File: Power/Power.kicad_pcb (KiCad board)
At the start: 2 copper layers, 34.8 x 23.1 mm, 53 parts, among them J1 Conn_01x04_Pin, J2 Conn_01x02, J3 Conn_01x06, J5 GND, J6 +BATT, Q2 AO3400A, Q3 AO3400A, Q4 AO3400A, U1 TPS54331DR, U2 XAL4030-682MEC, U3 TPS54331DR, U4 XAL4030-682MEC

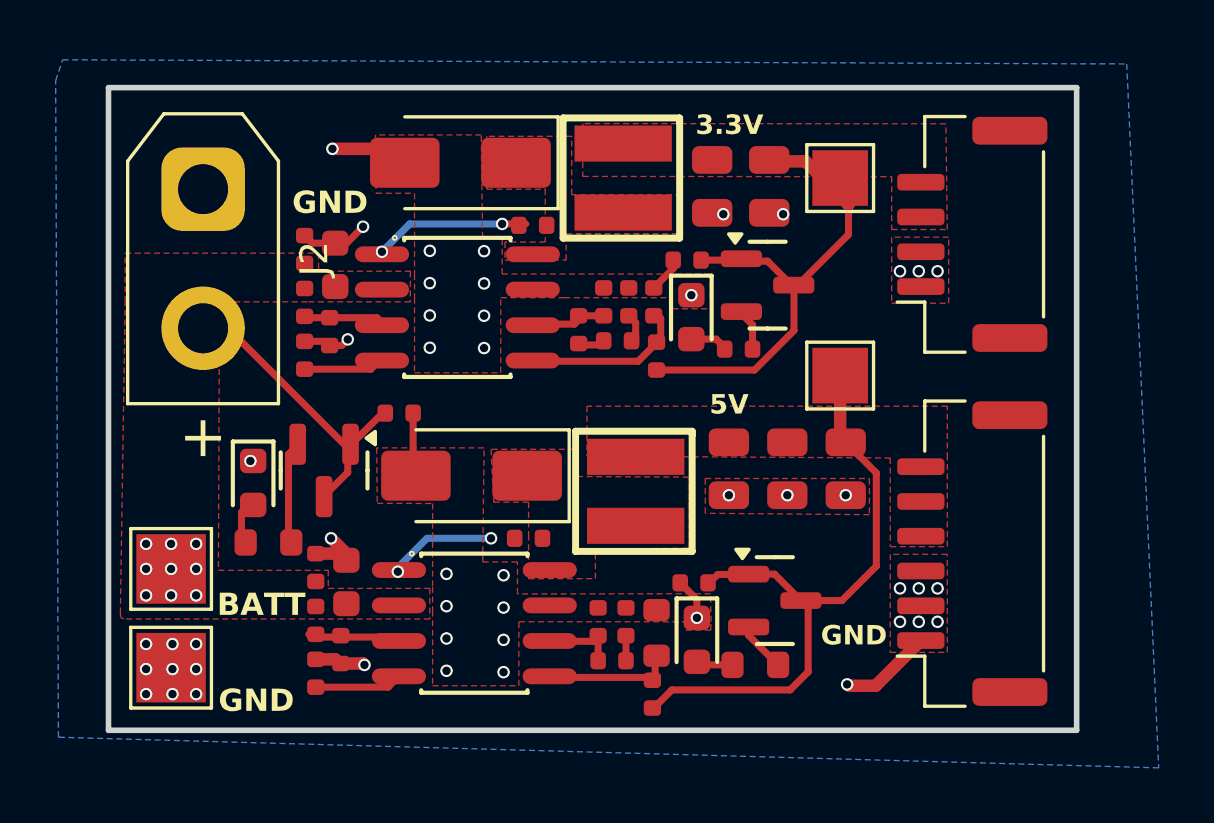
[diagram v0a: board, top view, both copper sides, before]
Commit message: feat: Added mounting holes, text and more connectors for PMU
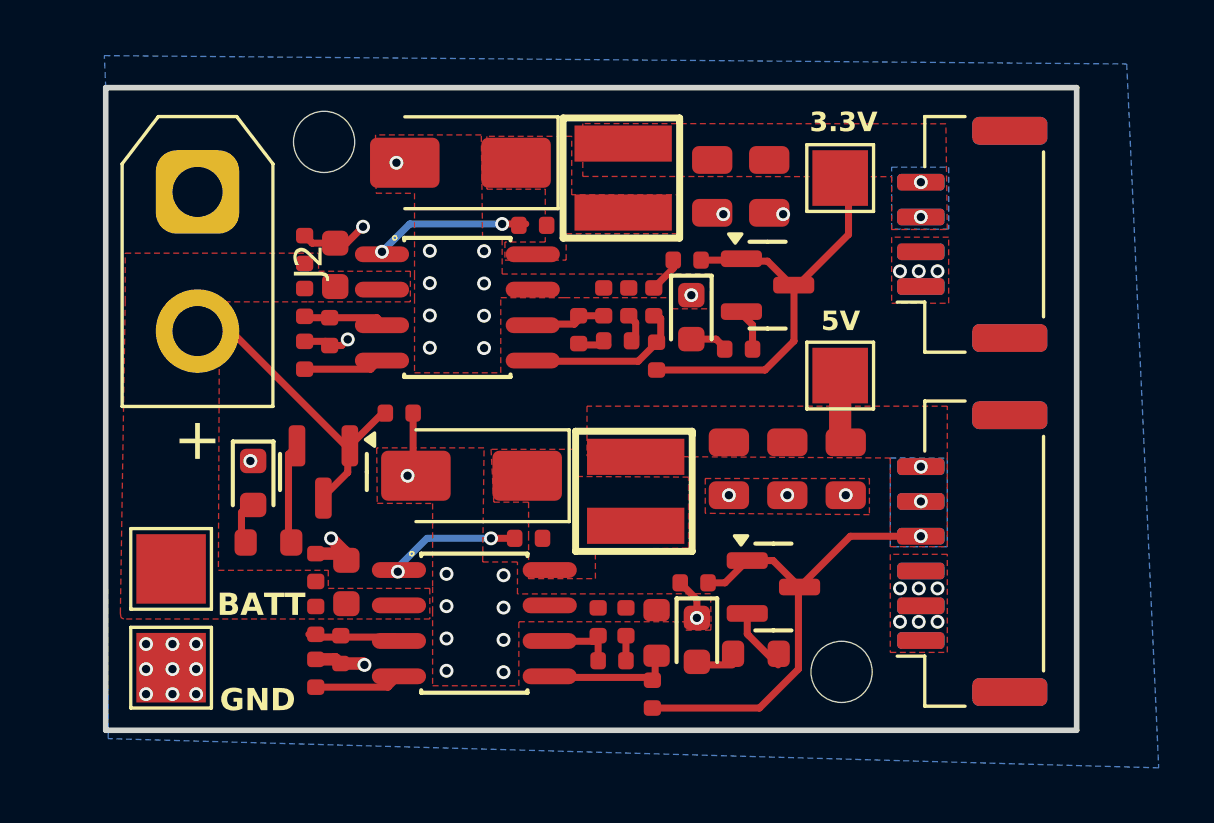
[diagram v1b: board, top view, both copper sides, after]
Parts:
- added ?: , , F.Cu at (121.0, 100.2)
- added ?: , , F.Cu at (102.4, 81.2)
- added J4: Conn_01x04_Pin, Connector_JST:JST_GH_SM04B-GHS-TB_1x04-1MP_P1.25mm_Horizontal, B.Cu at (125.7, 84.5)
- added J7: Conn_01x06, Connector_JST:JST_GH_SM06B-GHS-TB_1x06-1MP_P1.25mm_Horizontal, B.Cu at (125.7, 96.0)
- moved Q2 0.49 mm to (118.5, 97.2)
- moved R15 0.40 mm to (117.9, 99.5)
- moved J2 0.22 mm to (97.8, 83.0)
- moved Q3 0.06 mm to (102.4, 93.0)
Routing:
- net GND: track 19.7 -> 13.3 mm
- net 5V: track 23.4 -> 20.4 mm, vias 0 -> 3
- net +3.3V: track 17.7 -> 14.9 mm, vias 0 -> 2
- net Net-(U3-BOOT): track 4.01 -> 4.86 mm
- net Net-(Q2-S): track 1.80 -> 2.31 mm
- net +BATT: vias 9 -> 0
- added copper zone on B.Cu, net +3.3V
- added copper zone on B.Cu, net 5V
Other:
- board size 34.8 x 23.1 mm -> 34.9 x 23.1 mm
- board text added: "Maximum: 3A @ 3.3V, 5V"
- board text added: "STRATOSPHERE Power Management Unit"
